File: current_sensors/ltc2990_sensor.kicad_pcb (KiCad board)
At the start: 2 copper layers, 12.7 x 13.5 mm, 21 parts, among them U1 LTC2990

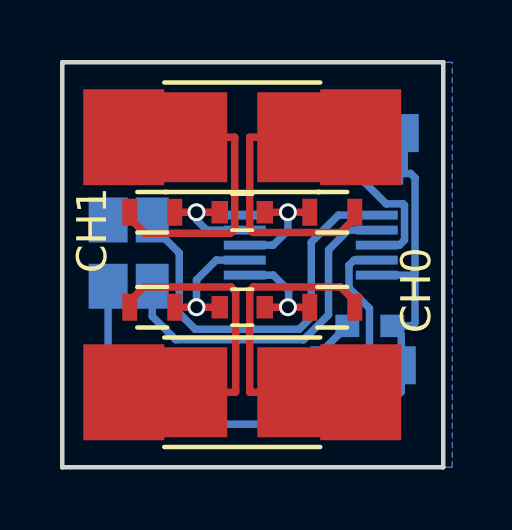
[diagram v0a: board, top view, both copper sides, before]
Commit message: Added ground pads to current sensor
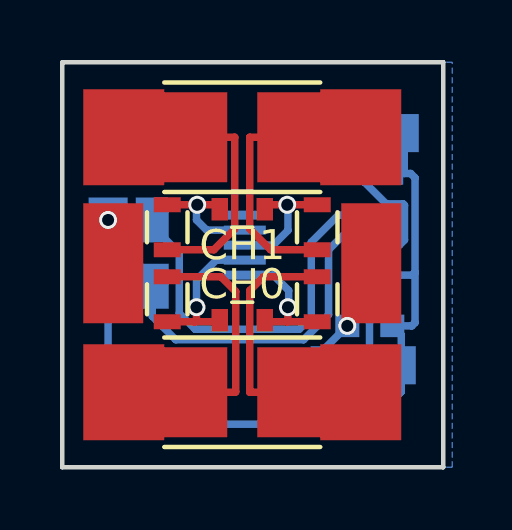
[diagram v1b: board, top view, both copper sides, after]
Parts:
- added W10: TEST_1P, Measurement_Points:Measurement_Point_Square-SMD-Pad_Big, F.Cu at (169.3, 116.2)
- added W9: TEST_1P, Measurement_Points:Measurement_Point_Square-SMD-Pad_Big, F.Cu at (160.7, 116.2)
- moved R3 0.71 mm to (167.5, 115.0), turned to 90 degrees
- moved R4 0.71 mm to (162.5, 115.0), turned to 90 degrees
- moved R5 0.57 mm to (162.5, 117.4), turned to 90 degrees
- moved R6 0.57 mm to (167.5, 117.4), turned to 90 degrees
- moved C3 0.43 mm to (165.0, 118.1)
- moved C2 0.10 mm to (165.0, 114.4)
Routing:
- net GND: track 1.62 -> 5.55 mm, vias 0 -> 2
- net Net-(R2-Pad2): track 9.12 -> 7.62 mm
- net Net-(R2-Pad1): track 9.09 -> 7.58 mm
- net Net-(R1-Pad1): track 10.7 -> 9.29 mm
- net Net-(R1-Pad2): track 10.7 -> 9.29 mm
- net Net-(C3-Pad2): track 4.29 -> 5.09 mm
- net Net-(C3-Pad1): track 3.74 -> 4.51 mm
- net Net-(C2-Pad2): track 3.51 -> 4.08 mm
- net Net-(C2-Pad1): track 3.75 -> 4.32 mm

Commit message: Redrawn the current sensor board
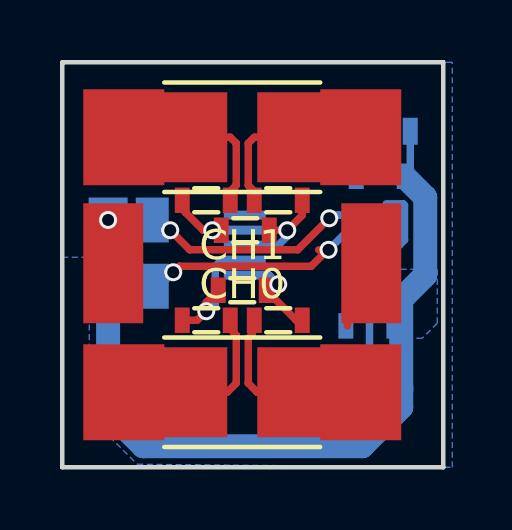
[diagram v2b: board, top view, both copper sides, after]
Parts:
- C1, C2, C3, C4: footprint Capacitors_SMD:C_0603 -> footprints:R_0603
- JP1, JP2: footprint Connect:GS3 -> footprints:GS3_SMALL
- R3, R4, R5, R6: footprint Resistors_SMD:R_0603 -> footprints:R_0603
- moved R3 1.58 mm to (166.2, 114.1), turned to 0 degrees
- moved R4 1.58 mm to (163.8, 114.1), turned to 180 degrees
- moved R5 1.48 mm to (163.8, 118.1), turned to 0 degrees
- moved R6 1.48 mm to (166.2, 118.1), turned to 180 degrees
- moved C3 1.00 mm to (165.0, 117.1)
- moved JP1 0.77 mm to (169.9, 111.8)
- moved C2 0.71 mm to (165.1, 115.1)
- moved C4 0.40 mm to (169.6, 113.3)
- moved JP2 0.34 mm to (169.3, 119.4)
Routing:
- net Net-(U1-Pad6): track 13.3 -> 8.37 mm, vias 0 -> 2
- net Net-(R1-Pad2): track 9.29 -> 5.82 mm
- net Net-(R1-Pad1): track 9.29 -> 5.82 mm
- net Net-(U1-Pad7): track 11.6 -> 8.59 mm, vias 0 -> 2
- net Net-(JP1-Pad2): track 5.45 -> 2.79 mm
- net VCC: track 25.4 -> 27.7 mm
- net Net-(R2-Pad2): track 7.62 -> 5.65 mm
- net Net-(R2-Pad1): track 7.58 -> 6.06 mm
- net Net-(C2-Pad2): track 4.08 -> 2.63 mm
- net Net-(C3-Pad1): track 4.51 -> 3.34 mm
- net GND: track 5.55 -> 5.22 mm, vias 2 -> 1
- added copper zone on B.Cu, net VCC

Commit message: Fixed minor mistakes on current sensor board
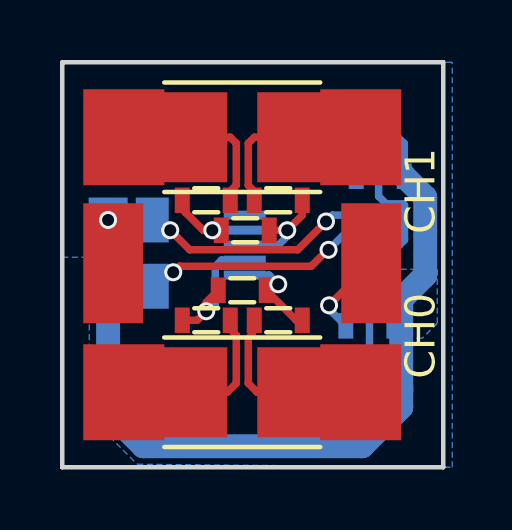
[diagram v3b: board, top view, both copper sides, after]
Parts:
- moved JP1 0.61 mm to (169.3, 111.8)
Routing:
- net Net-(JP1-Pad2): track 2.79 -> 5.42 mm
- net GND: track 5.22 -> 4.42 mm, vias 1 -> 2
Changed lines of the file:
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@@
   (general
     (links 32)
-    (no_connects 11)
-    (area 158.924999 109.424999 171.775001 123.075001)
+    (no_connects 0)
+    (area 157.552381 108.025 172.700001 124.575)
     (thickness 1.6)
     (drawings 5)
-    (tracks 113)
+    (tracks 119)
     (zones 0)
     (modules 23)
@@
     (38 B.Mask user hide)
     (39 F.Mask user hide)
-    (40 Dwgs.User user)
-    (41 Cmts.User user)
+    (40 Dwgs.User user hide)
+    (41 Cmts.User user hide)
     (42 Eco1.User user)
     (43 Eco2.User user hide)
@@
     (visible_elements 7FFFFF7F)
     (pcbplotparams
-      (layerselection 0x00030_80000001)
-      (usegerberextensions false)
+      (layerselection 0x010f0_80000001)
+      (usegerberextensions true)
+      (usegerberattributes true)
       (excludeedgelayer true)
       (linewidth 0.100000)
@@
       (effects (font (size 1 1) (thickness 0.15)))
     )
-    (fp_text value CH1 (at 0 3.6 180) (layer F.SilkS)
+    (fp_text value CH1 (at 5.942 1.792 270) (layer F.SilkS)
       (effects (font (size 1 1) (thickness 0.15)))
     )
@@
       (effects (font (size 1 1) (thickness 0.15)) (justify mirror))
     )
-    (fp_text value A1 (at 0 2.6 180) (layer B.SilkS)
+    (fp_text value A1 (at 0 -2.6125 180) (layer B.SilkS)
       (effects (font (size 1 1) (thickness 0.15)) (justify mirror))
     )
@@
   )
   (module footprints:GS3_SMALL (layer B.Cu)
-    (at 169.9 111.8 270)
+    (at 169.291 111.8 270)
     (descr "3-pin solder bridge")
     (tags "solder bridge")
@@
       (effects (font (size 1 1) (thickness 0.15)))
     )
-    (fp_text value CH0 (at 0 3.6 360) (layer F.SilkS)
+    (fp_text value CH0 (at -5.942 1.882 450) (layer F.SilkS)
       (effects (font (size 1 1) (thickness 0.15)))
     )
@@
   (gr_line (start 171.7 109.5) (end 171.7 123) (layer Edge.Cuts) (width 0.15))
   (gr_line (start 159 109.5) (end 171.7 109.5) (layer Edge.Cuts) (width 0.15))
-  (segment (start 170.6 111.8) (end 170.6 113.1) (width 0.25) (layer B.Cu) (net 1))
+  (segment (start 170.4 113.3) (end 170.4 112.209) (width 0.25) (layer B.Cu) (net 1))
+  (segment (start 170.4 112.209) (end 169.991 111.8) (width 0.25) (layer B.Cu) (net 1))
   (segment (start 170.6 113.1) (end 170.4 113.3) (width 0.25) (layer B.Cu) (net 1))
   (segment (start 170.3 120.485) (end 170.3 120.3) (width 0.25) (layer B.Cu) (net 1))
@@
   (segment (start 170.3 119.6) (end 170.3 118.5856) (width 0.25) (layer B.Cu) (net 1))
   (segment (start 170.3 118.5856) (end 170.0022 118.2878) (width 0.25) (layer B.Cu) (net 1))
-  (segment (start 169.3 116.2) (end 169.3 115.2) (width 0.25) (layer F.Cu) (net 2))
-  (segment (start 169.3 115.2) (end 169.1 115) (width 0.25) (layer F.Cu) (net 2))
-  (segment (start 168.5022 118.2878) (end 168.5022 116.9978) (width 0.25) (layer F.Cu) (net 2))
-  (segment (start 168.5022 116.9978) (end 169.3 116.2) (width 0.25) (layer F.Cu) (net 2))
+  (segment (start 167.894 117.602) (end 167.894 117.7296) (width 0.25) (layer B.Cu) (net 2))
+  (segment (start 167.894 117.7296) (end 168.4522 118.2878) (width 0.25) (layer B.Cu) (net 2))
+  (segment (start 169.3 116.2) (end 169.296 116.2) (width 0.25) (layer F.Cu) (net 2))
+  (segment (start 169.296 116.2) (end 167.894 117.602) (width 0.25) (layer F.Cu) (net 2))
+  (via (at 167.894 117.602) (size 0.6) (drill 0.4) (layers F.Cu B.Cu) (net 2))
   (segment (start 160.7 116.2) (end 160.7 114.9292) (width 0.25) (layer F.Cu) (net 2))
   (segment (start 160.7 114.9292) (end 160.528 114.7572) (width 0.25) (layer F.Cu) (net 2))
@@
   (segment (start 165.089 115.6) (end 165.0844 115.5954) (width 0.25) (layer B.Cu) (net 3))
   (segment (start 165.0844 115.5954) (end 166.0344 115.5954) (width 0.25) (layer B.Cu) (net 3))
+  (segment (start 164 115.1) (end 164.3 115.1) (width 0.25) (layer F.Cu) (net 4))
   (segment (start 163.7 115.1) (end 164 115.1) (width 0.25) (layer F.Cu) (net 4))
   (segment (start 165.0844 115.0954) (end 164.0046 115.0954) (width 0.25) (layer B.Cu) (net 4))
@@
   (via (at 163.8 117.8) (size 0.6) (drill 0.4) (layers F.Cu B.Cu) (net 6))
   (segment (start 165.0844 116.0954) (end 164.3046 116.0954) (width 0.25) (layer B.Cu) (net 6))
+  (segment (start 169.545 112.459002) (end 169.545 113.968002) (width 0.25) (layer B.Cu) (net 7))
+  (segment (start 169.545 113.968002) (end 169.797397 114.220399) (width 0.25) (layer B.Cu) (net 7))
+  (segment (start 169.291 111.8) (end 169.291 112.205002) (width 0.25) (layer B.Cu) (net 7))
+  (segment (start 169.291 112.205002) (end 169.545 112.459002) (width 0.25) (layer B.Cu) (net 7))
   (segment (start 170.409401 115.425401) (end 170.239402 115.5954) (width 0.25) (layer B.Cu) (net 7))
   (segment (start 169.797397 114.220399) (end 170.364401 114.220399) (width 0.25) (layer B.Cu) (net 7))
@@
   (segment (start 165.4 114.1) (end 165.4 113.8) (width 0.25) (layer F.Cu) (net 10))
   (segment (start 168.95 112) (end 167 112) (width 0.25) (layer F.Cu) (net 10))
+  (segment (start 167 120.5) (end 168.95 120.5) (width 0.25) (layer F.Cu) (net 11))
   (segment (start 165.324999 118.575001) (end 165.324999 118.175001) (width 0.25) (layer F.Cu) (net 11))
   (segment (start 165.324999 118.175001) (end 165.4 118.1) (width 0.25) (layer F.Cu) (net 11))
-  (segment (start 167 120.5) (end 168.95 120.5) (width 0.25) (layer F.Cu) (net 11))
   (segment (start 165.2 120.2) (end 165.5 120.5) (width 0.25) (layer F.Cu) (net 11))
   (segment (start 165.5 120.5) (end 167 120.5) (width 0.25) (layer F.Cu) (net 11))
@@
   (segment (start 164.8 120.2) (end 164.5 120.5) (width 0.25) (layer F.Cu) (net 12))
   (segment (start 164.675001 118.475001) (end 164.8 118.6) (width 0.25) (layer F.Cu) (net 12))
-  (segment (start 167.9 114.7) (end 166.849999 115.750001) (width 0.25) (layer F.Cu) (net 13))
+  (via (at 167.792 114.808) (size 0.6) (drill 0.4) (layers F.Cu B.Cu) (net 13))
+  (segment (start 167.792 114.808) (end 166.849999 115.750001) (width 0.25) (layer F.Cu) (net 13))
+  (segment (start 169.4844 114.5954) (end 168.0046 114.5954) (width 0.25) (layer B.Cu) (net 13))
+  (segment (start 168.0046 114.5954) (end 167.9 114.7) (width 0.25) (layer B.Cu) (net 13))
+  (segment (start 167.9 114.7) (end 167.792 114.808) (width 0.25) (layer B.Cu) (net 13))
   (segment (start 166.849999 115.750001) (end 163.250001 115.750001) (width 0.25) (layer F.Cu) (net 13))
   (segment (start 163.250001 115.750001) (end 162.6 115.1) (width 0.25) (layer F.Cu) (net 13))
@@
   (segment (start 162.2572 114.7572) (end 162.6 115.1) (width 0.25) (layer B.Cu) (net 13))
   (via (at 162.6 115.1) (size 0.6) (drill 0.4) (layers F.Cu B.Cu) (net 13))
-  (segment (start 168.2046 114.5954) (end 168.0046 114.5954) (width 0.25) (layer B.Cu) (net 13))
-  (segment (start 168.0046 114.5954) (end 167.9 114.7) (width 0.25) (layer B.Cu) (net 13))
-  (via (at 167.9 114.7) (size 0.6) (drill 0.4) (layers F.Cu B.Cu) (net 13))
-  (segment (start 169.4844 114.5954) (end 168.2046 114.5954) (width 0.25) (layer B.Cu) (net 13))
   (segment (start 162.7 116.5) (end 162.233 116.967) (width 0.25) (layer B.Cu) (net 14))
   (segment (start 162.233 116.967) (end 162 116.967) (width 0.25) (layer B.Cu) (net 14))
@@
   (segment (start 167.847399 115.752601) (end 167.3 116.3) (width 0.25) (layer F.Cu) (net 14))
   (segment (start 167.877199 115.752601) (end 167.847399 115.752601) (width 0.25) (layer F.Cu) (net 14))
-  (segment (start 167.877199 115.752601) (end 167.547399 115.752601) (width 0.25) (layer F.Cu) (net 14))
   (via (at 167.877199 115.752601) (size 0.6) (drill 0.4) (layers F.Cu B.Cu) (net 14))
   (segment (start 168.5344 115.0954) (end 169.4844 115.0954) (width 0.25) (layer B.Cu) (net 14))
